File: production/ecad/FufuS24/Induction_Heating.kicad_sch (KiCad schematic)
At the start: 16 parts, among them IC1 FOD3150, J1 Conn_01x02, U3 STGP8NC60KD

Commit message: updated footprint library
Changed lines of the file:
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@@
+    (effects (font (size 1.27 1.27)) (justify left top))
+  )
+  (text_box "Updated C18 to be ~0.766uF\n"
+    (at 199.39 62.23 0) (size 17.78 5.08)
+    (stroke (width 0) (type default))
+    (fill (type none))
     (effects (font (size 1.27 1.27)) (justify left top))
   )

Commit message: worked on power page
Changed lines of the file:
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@@
     (stroke (width 0) (type default))
   )
-  (wire (pts (xy 133.985 96.52) (xy 137.795 96.52))
-    (stroke (width 0) (type default))
-  )
-  (wire (pts (xy 133.985 88.9) (xy 133.985 96.52))
+  (wire (pts (xy 133.35 96.52) (xy 137.795 96.52))
+    (stroke (width 0) (type default))
+  )
+  (wire (pts (xy 133.35 88.9) (xy 133.35 96.52))
     (stroke (width 0) (type default))
   )
@@
     )
   )
-  (symbol (lib_id "more_powerSymbols:+16V") (at 133.985 88.9 0) (unit 1)
+  (symbol (lib_id "more_powerSymbols:+16V") (at 133.35 88.9 0) (unit 1)
     (in_bom no) (on_board no) (dnp no) (fields_autoplaced)
-    (property "Reference" "#PWR018" (at 133.985 83.82 0)
-      (effects (font (size 1.27 1.27)) hide)
-    )
-    (property "Value" "~" (at 133.985 88.9 0)
-      (effects (font (size 1.27 1.27)))
-    )
-    (property "Footprint" "" (at 133.985 88.9 0)
-      (effects (font (size 1.27 1.27)) hide)
-    )
-    (property "Datasheet" "" (at 133.985 88.9 0)
-      (effects (font (size 1.27 1.27)) hide)
-    )
+    (property "Reference" "#PWR018" (at 133.35 83.82 0)
+      (effects (font (size 1.27 1.27)) hide)
+    )
+    (property "Value" "~" (at 133.35 88.9 0)
+      (effects (font (size 1.27 1.27)))
+    )
+    (property "Footprint" "" (at 133.35 88.9 0)
+      (effects (font (size 1.27 1.27)) hide)
+    )
+    (property "Datasheet" "" (at 133.35 88.9 0)
+      (effects (font (size 1.27 1.27)) hide)
+    )

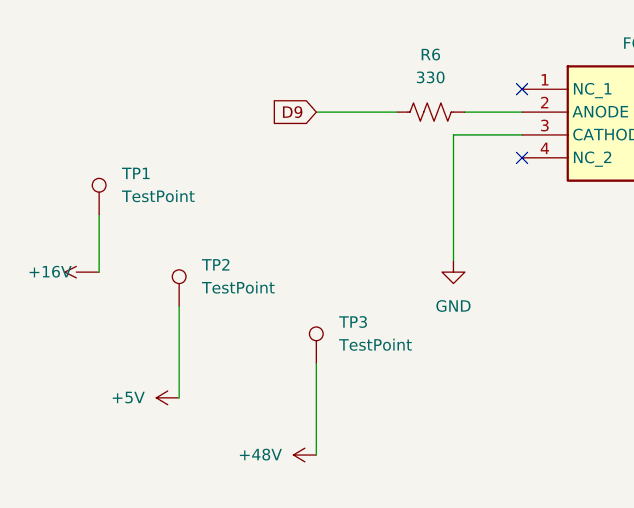
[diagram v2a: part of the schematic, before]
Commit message: Finished first draft of power page
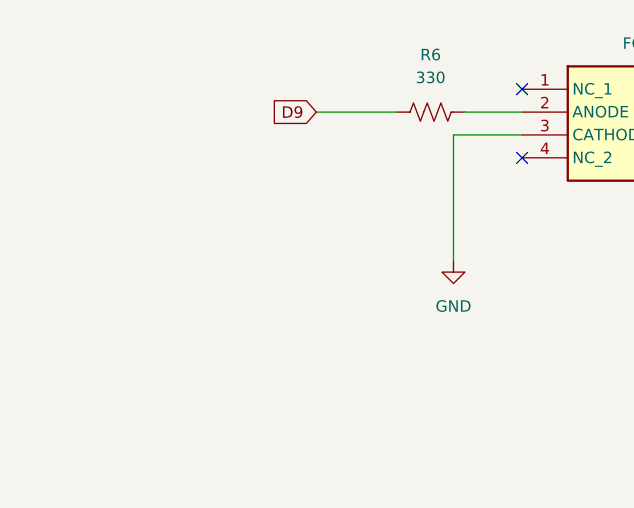
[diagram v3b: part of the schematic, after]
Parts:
- removed TP1, TP2, TP3: TestPoint, TestPoint:TestPoint_Pad_2.0x2.0mm, symbol Connector:TestPoint
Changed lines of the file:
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@@
-    (stroke (width 0) (type default))
-  )
-  (wire (pts (xy 69.215 130.81) (xy 69.215 140.97))
     (stroke (width 0) (type default))
   )
@@
     (stroke (width 0) (type default))
   )
-  (wire (pts (xy 60.325 120.65) (xy 60.325 127))
-    (stroke (width 0) (type default))
-  )
   (wire (pts (xy 154.305 109.22) (xy 154.305 121.92))
     (stroke (width 0) (type default))
@@
   )
   (wire (pts (xy 188.595 53.34) (xy 188.595 60.96))
-    (stroke (width 0) (type default))
-  )
-  (wire (pts (xy 84.455 137.16) (xy 84.455 147.32))
     (stroke (width 0) (type default))
   )
@@
     )
   )
-  (symbol (lib_id "power:+5V") (at 69.215 140.97 90) (unit 1)
-    (in_bom yes) (on_board yes) (dnp no) (fields_autoplaced)
-    (property "Reference" "#PWR015" (at 73.025 140.97 0)
-      (effects (font (size 1.27 1.27)) hide)
-    )
-    (property "Value" "+5V" (at 65.405 140.97 90)
-      (effects (font (size 1.27 1.27)) (justify left))
-    )
-    (property "Footprint" "" (at 69.215 140.97 0)
-      (effects (font (size 1.27 1.27)) hide)
-    )
-    (property "Datasheet" "" (at 69.215 140.97 0)
-      (effects (font (size 1.27 1.27)) hide)
-    )
-    (pin "1")
-    (instances
-      (project "FufuS24"
-        (path "/c4c3980b-c8c0-435e-abdc-bbed2349d7ac/57fb5dcd-e779-40d3-8741-57c7eee1ca58"
-          (reference "#PWR015") (unit 1)
-        )
-      )
-    )
-  )
   (symbol (lib_id "power:GND") (at 189.865 144.78 0) (unit 1)
     (in_bom yes) (on_board yes) (dnp no) (fields_autoplaced)
@@
         (path "/c4c3980b-c8c0-435e-abdc-bbed2349d7ac/57fb5dcd-e779-40d3-8741-57c7eee1ca58"
           (reference "#PWR017") (unit 1)
-        )
-      )
-    )
-  )
-  (symbol (lib_id "Connector:TestPoint") (at 60.325 120.65 0) (unit 1)
-    (in_bom yes) (on_board yes) (dnp no) (fields_autoplaced)
-    (property "Reference" "TP1" (at 62.865 116.078 0)
-      (effects (font (size 1.27 1.27)) (justify left))
-    )
-    (property "Value" "TestPoint" (at 62.865 118.618 0)
-      (effects (font (size 1.27 1.27)) (justify left))
-    )
-    (property "Footprint" "TestPoint:TestPoint_Pad_2.0x2.0mm" (at 65.405 120.65 0)
-      (effects (font (size 1.27 1.27)) hide)
-    )
-    (property "Datasheet" "~" (at 65.405 120.65 0)
-      (effects (font (size 1.27 1.27)) hide)
-    )
-    (pin "1")
-    (instances
-      (project "FufuS24"
-        (path "/c4c3980b-c8c0-435e-abdc-bbed2349d7ac/57fb5dcd-e779-40d3-8741-57c7eee1ca58"
-          (reference "TP1") (unit 1)
         )
       )
@@
     )
   )
-  (symbol (lib_id "Connector:TestPoint") (at 69.215 130.81 0) (unit 1)
-    (in_bom yes) (on_board yes) (dnp no) (fields_autoplaced)
-    (property "Reference" "TP2" (at 71.755 126.238 0)
-      (effects (font (size 1.27 1.27)) (justify left))
-    )
-    (property "Value" "TestPoint" (at 71.755 128.778 0)
-      (effects (font (size 1.27 1.27)) (justify left))
-    )
-    (property "Footprint" "TestPoint:TestPoint_Pad_2.0x2.0mm" (at 74.295 130.81 0)
-      (effects (font (size 1.27 1.27)) hide)
-    )
-    (property "Datasheet" "~" (at 74.295 130.81 0)
-      (effects (font (size 1.27 1.27)) hide)
-    )
-    (pin "1")
-    (instances
-      (project "FufuS24"
-        (path "/c4c3980b-c8c0-435e-abdc-bbed2349d7ac/57fb5dcd-e779-40d3-8741-57c7eee1ca58"
-          (reference "TP2") (unit 1)
-        )
-      )
-    )
-  )
   (symbol (lib_id "power:GND") (at 161.925 73.66 0) (unit 1)
     (in_bom yes) (on_board yes) (dnp no) (fields_autoplaced)
@@
     )
   )
-  (symbol (lib_id "more_powerSymbols:+16V") (at 60.325 127 90) (unit 1)
-    (in_bom no) (on_board no) (dnp no) (fields_autoplaced)
-    (property "Reference" "#PWR014" (at 55.245 127 0)
-      (effects (font (size 1.27 1.27)) hide)
-    )
-    (property "Value" "~" (at 60.325 127 0)
-      (effects (font (size 1.27 1.27)))
-    )
-    (property "Footprint" "" (at 60.325 127 0)
-      (effects (font (size 1.27 1.27)) hide)
-    )
-    (property "Datasheet" "" (at 60.325 127 0)
-      (effects (font (size 1.27 1.27)) hide)
-    )
-    (pin "")
-    (instances
-      (project "FufuS24"
-        (path "/c4c3980b-c8c0-435e-abdc-bbed2349d7ac/57fb5dcd-e779-40d3-8741-57c7eee1ca58"
-          (reference "#PWR014") (unit 1)
-        )
-      )
-    )
-  )
   (symbol (lib_id "Device:R_US") (at 144.78 109.22 90) (unit 1)
     (in_bom yes) (on_board yes) (dnp no) (fields_autoplaced)
@@
         )
       )
-    )
-  )
-  (symbol (lib_id "power:+48V") (at 84.455 147.32 90) (unit 1)
-    (in_bom yes) (on_board yes) (dnp no) (fields_autoplaced)
-    (property "Reference" "#PWR016" (at 88.265 147.32 0)
-      (effects (font (size 1.27 1.27)) hide)
-    )
-    (property "Value" "+48V" (at 80.645 147.32 90)
-      (effects (font (size 1.27 1.27)) (justify left))
-    )
-    (property "Footprint" "" (at 84.455 147.32 0)
-      (effects (font (size 1.27 1.27)) hide)
-    )
-    (property "Datasheet" "" (at 84.455 147.32 0)
-      (effects (font (size 1.27 1.27)) hide)
-    )
-    (pin "1")
-    (instances
-      (project "FufuS24"
-        (path "/c4c3980b-c8c0-435e-abdc-bbed2349d7ac/57fb5dcd-e779-40d3-8741-57c7eee1ca58"
-          (reference "#PWR016") (unit 1)
-        )
-      )
-    )
-  )
-  (symbol (lib_id "Connector:TestPoint") (at 84.455 137.16 0) (unit 1)
-    (in_bom yes) (on_board yes) (dnp no) (fields_autoplaced)
-    (property "Reference" "TP3" (at 86.995 132.588 0)
-      (effects (font (size 1.27 1.27)) (justify left))
-    )
-    (property "Value" "TestPoint" (at 86.995 135.128 0)
-      (effects (font (size 1.27 1.27)) (justify left))
-    )
-    (property "Footprint" "TestPoint:TestPoint_Pad_2.0x2.0mm" (at 89.535 137.16 0)
-      (effects (font (size 1.27 1.27)) hide)
-    )
-    (property "Datasheet" "~" (at 89.535 137.16 0)
-      (effects (font (size 1.27 1.27)) hide)
-    )
-    (pin "1")
-    (instances
-      (project "FufuS24"
-        (path "/c4c3980b-c8c0-435e-abdc-bbed2349d7ac/57fb5dcd-e779-40d3-8741-57c7eee1ca58"
-          (reference "TP3") (unit 1)
-        )
-      )

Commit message: Efan
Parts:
- added C34: C, symbol Device:C
- added D1: LED, symbol Device:LED
- added D2: 1N4001, Diode_THT:D_DO-41_SOD81_P10.16mm_Horizontal, symbol Diode:1N4001
- added R19: R_US, symbol Device:R_US
- added U8: AD8561, symbol Comparator:AD8561
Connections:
- net GND: now also C34.2, U8.6 (GND)
- new net: C34.1, D2.1 (K), R19.1, U8.1 (V+)
- new net: D1.2 (A), R19.2
- new net: D1.1 (K), U8.7 (Q)
- new net +5V: D2.2 (A)
- new net TEMP_DAT: U8.3 (-)
- new net V_REF: U8.2 (+)

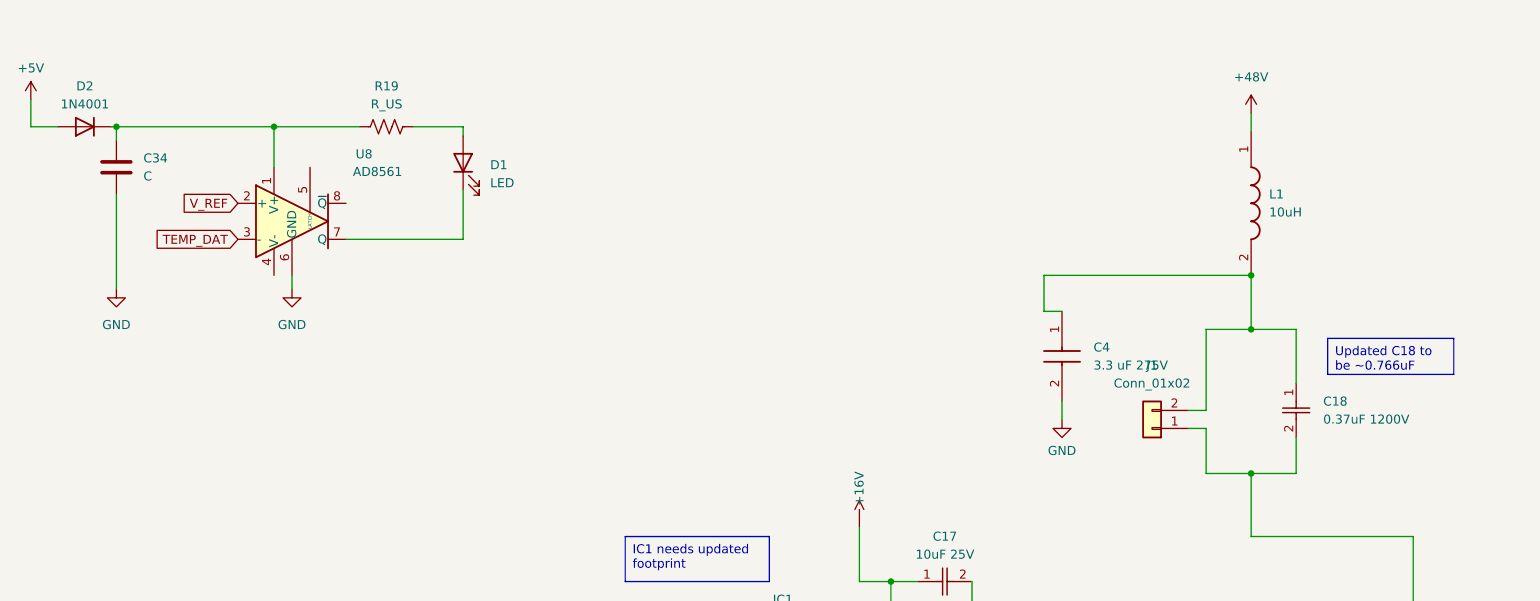
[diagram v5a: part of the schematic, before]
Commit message: Updated heating cap
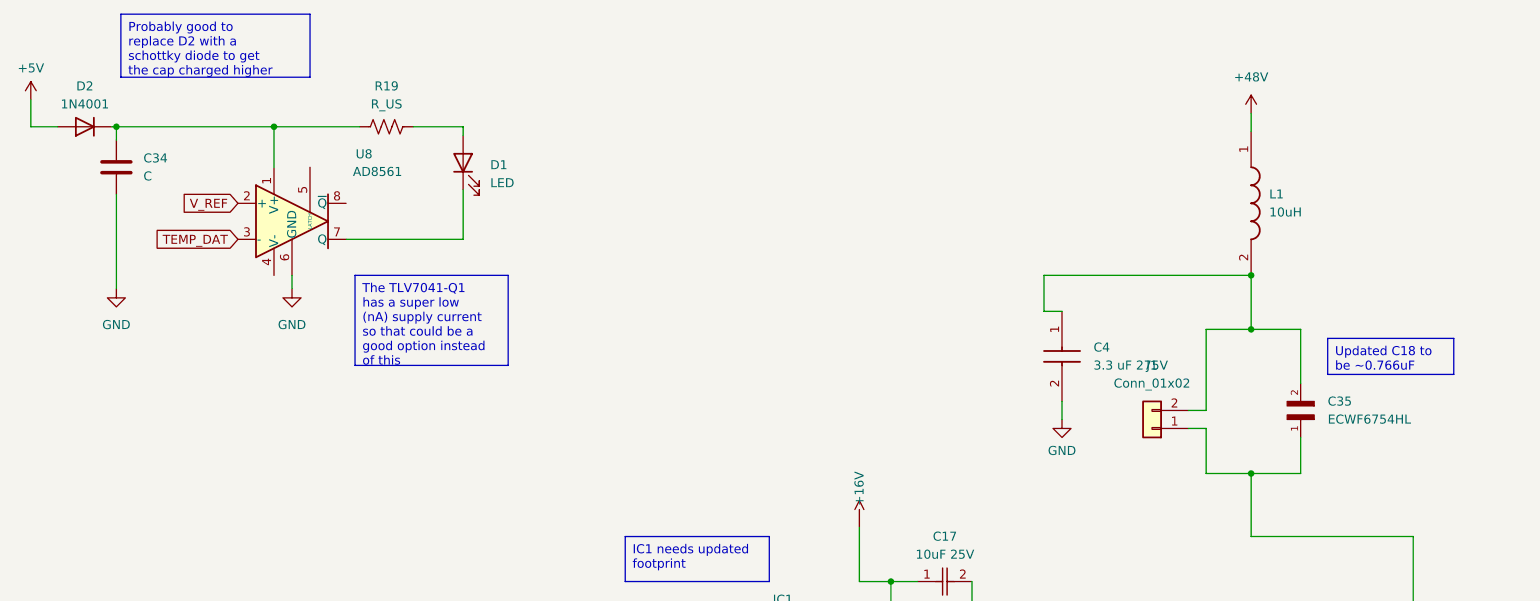
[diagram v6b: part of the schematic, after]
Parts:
- removed C18: 0.37uF 1200V, ECWfootprints:CAP_ECWFL_STRAIGHT_20.5LX11.9TX18.5H_PAN, symbol 2023-11-09_20-58-51:ECW-F6364JL
- added C35: ECWF6754HL, ECWF6754HL:CAPRR2500W80L2800T1330H1990, symbol ECWF6754HL:ECWF6754HL
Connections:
- net at C4.1, J1.2 (Pin_2), L1.2: now also C35.2
- net at J1.1 (Pin_1), U3.2 (C): now also C35.1
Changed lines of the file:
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@@
     (stroke (width 0) (type default))
   )
-  (wire (pts (xy 194.945 76.2) (xy 194.945 81.28))
+  (wire (pts (xy 195.58 76.2) (xy 195.58 81.28))
     (stroke (width 0) (type default))
   )
@@
     (stroke (width 0) (type default))
   )
-  (wire (pts (xy 188.595 60.96) (xy 194.945 60.96))
+  (wire (pts (xy 188.595 60.96) (xy 195.58 60.96))
     (stroke (width 0) (type default))
   )
@@
     (stroke (width 0) (type default))
   )
-  (wire (pts (xy 188.595 81.28) (xy 194.945 81.28))
+  (wire (pts (xy 188.595 81.28) (xy 195.58 81.28))
     (stroke (width 0) (type default))
   )
@@
     (stroke (width 0) (type default))
   )
-  (wire (pts (xy 194.945 60.96) (xy 194.945 68.58))
+  (wire (pts (xy 195.58 60.96) (xy 195.58 68.58))
     (stroke (width 0) (type default))
   )
@@
   (wire (pts (xy 189.865 130.81) (xy 205.105 130.81))
     (stroke (width 0) (type default))
+  )
+  (text_box "Probably good to replace D2 with a schottky diode to get the cap charged higher"
+    (at 29.21 16.51 0) (size 26.67 8.89)
+    (stroke (width 0) (type default))
+    (fill (type none))
+    (effects (font (size 1.27 1.27)) (justify left top))
+  )
+  (text_box "The TLV7041-Q1 has a super low (nA) supply current so that could be a good option instead of this\n"
+    (at 62.23 53.34 0) (size 21.59 12.7)
+    (stroke (width 0) (type default))
+    (fill (type none))
+    (effects (font (size 1.27 1.27)) (justify left top))
   )
   (text_box "IC1 needs updated footprint\n"
@@
     (property "Intersheetrefs" "${INTERSHEET_REFS}" (at 210.3883 130.81 0)
       (effects (font (size 1.27 1.27)) (justify left) hide)
-    )
-  )
-  (symbol (lib_id "2023-11-09_20-58-51:ECW-F6364JL") (at 194.945 68.58 270) (unit 1)
-    (in_bom yes) (on_board yes) (dnp no) (fields_autoplaced)
-    (property "Reference" "C18" (at 198.755 71.12 90)
-      (effects (font (size 1.27 1.27)) (justify left))
-    )
-    (property "Value" "0.37uF 1200V" (at 198.755 73.66 90)
-      (effects (font (size 1.27 1.27)) (justify left))
-    )
-    (property "Footprint" "ECWfootprints:CAP_ECWFL_STRAIGHT_20.5LX11.9TX18.5H_PAN" (at 194.945 68.58 0)
-      (effects (font (size 1.27 1.27) italic) hide)
-    )
-    (property "Datasheet" "ECW-F6364JL" (at 194.945 68.58 0)
-      (effects (font (size 1.27 1.27) italic) hide)
-    )
-    (pin "1")
-    (pin "2")
-    (instances
-      (project "FufuS24"
-        (path "/c4c3980b-c8c0-435e-abdc-bbed2349d7ac/57fb5dcd-e779-40d3-8741-57c7eee1ca58"
-          (reference "C18") (unit 1)
-        )
-      )
     )
   )
@@
         )
       )
+    )
+  )
+  (symbol (lib_id "ECWF6754HL:ECWF6754HL") (at 195.58 73.66 90) (unit 1)
+    (in_bom yes) (on_board yes) (dnp no) (fields_autoplaced)
+    (property "Reference" "C35" (at 199.39 71.12 90)
+      (effects (font (size 1.27 1.27)) (justify right))
+    )
+    (property "Value" "ECWF6754HL" (at 199.39 73.66 90)
+      (effects (font (size 1.27 1.27)) (justify right))
+    )
+    (property "Footprint" "ECWF6754HL:CAPRR2500W80L2800T1330H1990" (at 195.58 73.66 0)
+      (effects (font (size 1.27 1.27)) (justify bottom) hide)
+    )
+    (property "Datasheet" "" (at 195.58 73.66 0)
+      (effects (font (size 1.27 1.27)) hide)
+    )
+    (property "PARTREV" "11-Oct-17" (at 195.58 73.66 0)
+      (effects (font (size 1.27 1.27)) (justify bottom) hide)
+    )
+    (property "STANDARD" "IPC-7351B" (at 195.58 73.66 0)
+      (effects (font (size 1.27 1.27)) (justify bottom) hide)
+    )
+    (property "MAXIMUM_PACKAGE_HEIGHT" "19.9 mm" (at 195.58 73.66 0)
+      (effects (font (size 1.27 1.27)) (justify bottom) hide)
+    )
+    (property "MANUFACTURER" "Panasonic" (at 195.58 73.66 0)
+      (effects (font (size 1.27 1.27)) (justify bottom) hide)
+    )
+    (pin "1")
+    (pin "2")
+    (instances
+      (project "FufuS24"
+        (path "/c4c3980b-c8c0-435e-abdc-bbed2349d7ac/57fb5dcd-e779-40d3-8741-57c7eee1ca58"
+          (reference "C35") (unit 1)
+        )
+      )
